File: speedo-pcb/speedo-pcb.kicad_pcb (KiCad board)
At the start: 4 copper layers, 52 x 52 mm, 60 parts, among them J1 Debug, J2 Mode, J3 Speedo, J4 Power, J5 VBAT, J6 BOOT, J7 Breakout, M1 X27_128, U1 XC6206P332MR, U3 OLED_128x32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

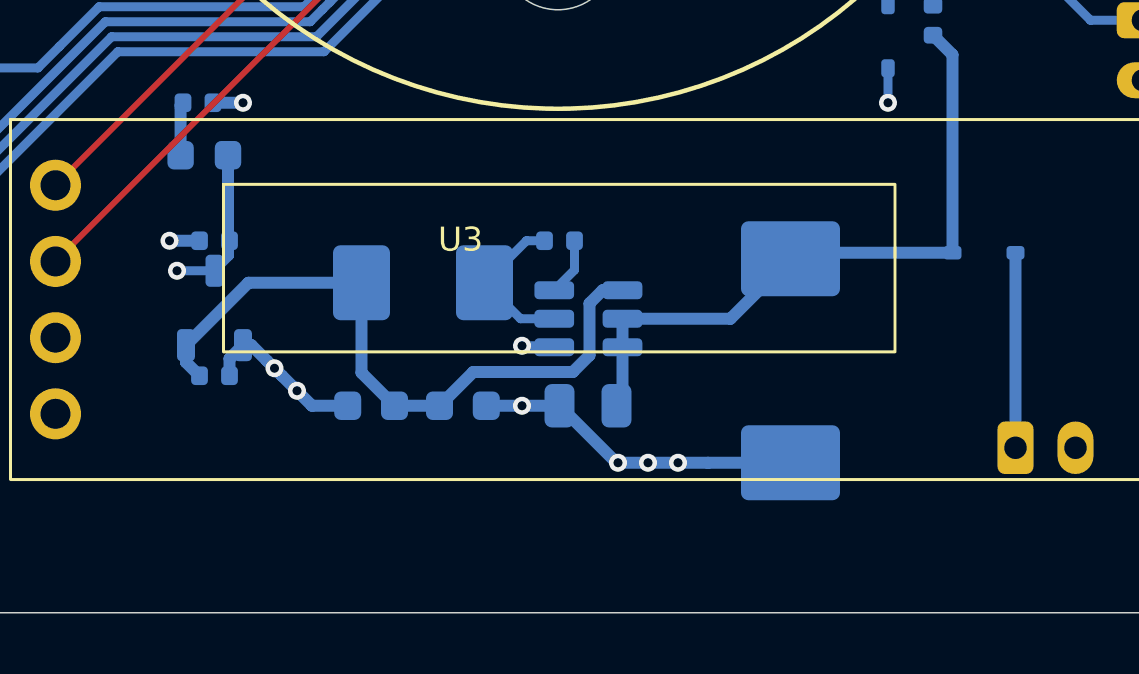
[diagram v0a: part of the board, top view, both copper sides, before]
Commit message: buck converter and tvs
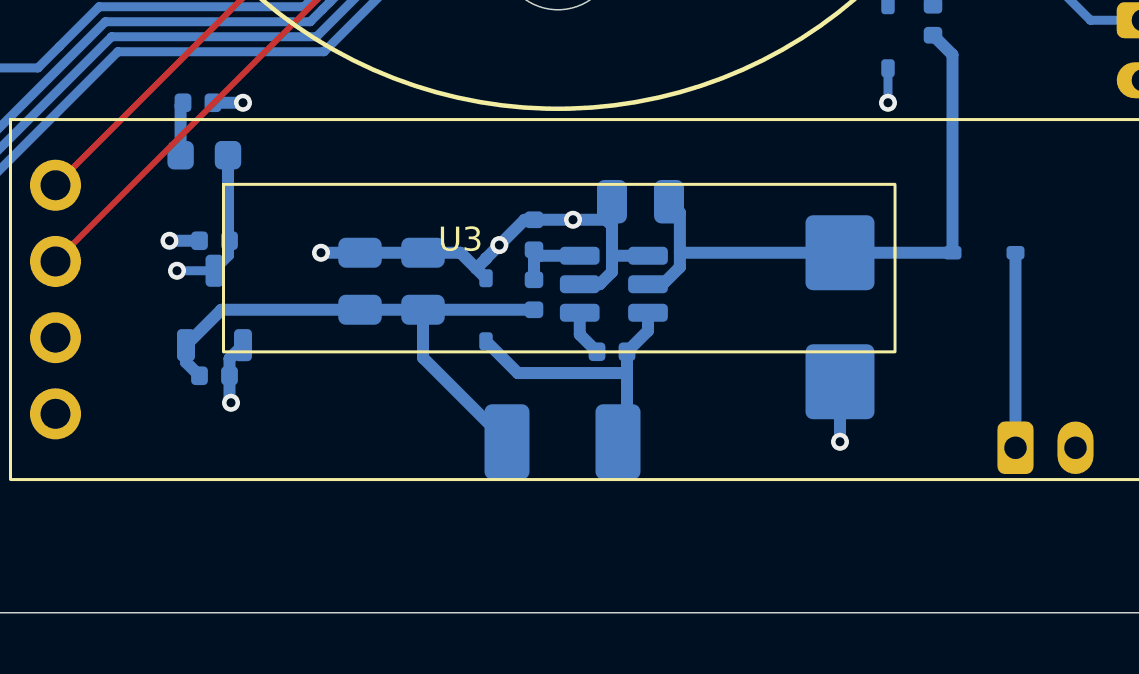
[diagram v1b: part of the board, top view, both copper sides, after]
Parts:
- removed C6: 22uF, PCM_JLCPCB:C_0603
- removed L2: 4.7uH, Inductor_SMD:L_Chilisin_BMRA00050520
- removed U5: AP63205WU, Package_TO_SOT_SMD:TSOT-23-6
- added C20: 22uF, PCM_JLCPCB:C_0805, B.Cu at (93.4, 115.0)
- added D14: P6SMB6.8CA/TR13, PCM_JLCPCB:D_SMB, B.Cu at (109.4, 116.2)
- added L1: FXL0420-100-M, Inductor_SMD:L_Sunlord_MWSA0402S, B.Cu at (100.2, 120.3)
- added R4: 10kΩ, PCM_JLCPCB:R_0402, B.Cu at (99.2, 115.4)
- added R7: 2kΩ, PCM_JLCPCB:R_0402, B.Cu at (99.2, 113.4)
- added U6: LGS5145, Package_TO_SOT_SMD:SOT-23-6, B.Cu at (101.9, 115.0)
- C5: value 22uF -> 10uF; footprint PCM_JLCPCB:C_0603 -> PCM_JLCPCB:C_0805
- D12: value SMCJ18CA -> 1N5819WS; footprint PCM_JLCPCB:D_SMC -> PCM_JLCPCB:D_SOD-323
- moved D12 10.3 mm to (97.6, 115.9)
- moved C4 7.02 mm to (102.8, 112.3)
- moved C5 4.36 mm to (95.5, 115.0), turned to 90 degrees
- moved C1 4.09 mm to (101.8, 117.3)
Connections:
- C1 pad 2: Net-(U5-BST) -> Net-(U6-SW)
- D12 pad 1: GND -> Net-(U6-SW)
- D12 pad 2: +12V -> GND
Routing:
- net Net-(U6-SW): track 0.00 -> 9.86 mm
- net Net-(U6-BST): track 5.40 -> 1.54 mm
- net +5V: track 22.7 -> 18.9 mm
- net Net-(U6-FB): track 0.00 -> 2.61 mm
- net GND: track 51.1 -> 53.6 mm, vias 24 -> 22
- net Net-(U5-BST): track 1.93 -> 0.00 mm
- net +12V: track 22.1 -> 20.2 mm

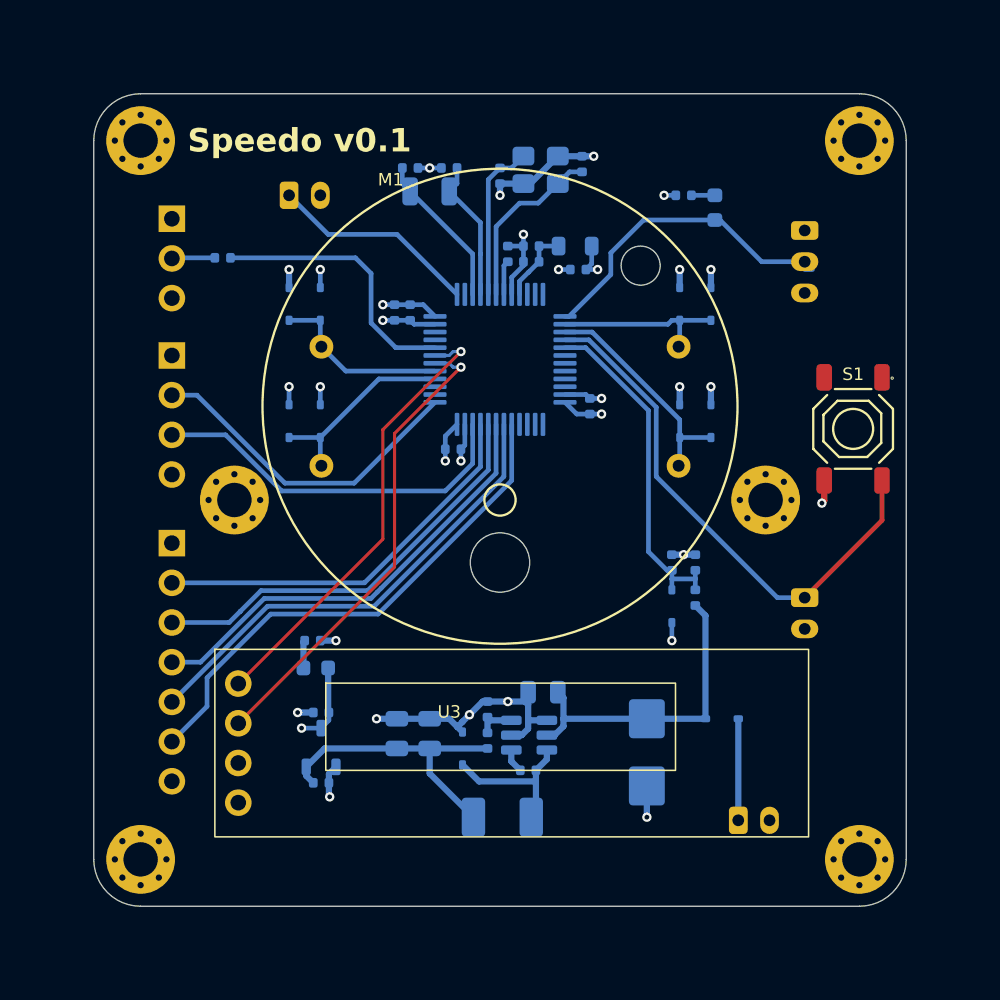
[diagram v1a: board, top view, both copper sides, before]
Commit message: buck converter fills
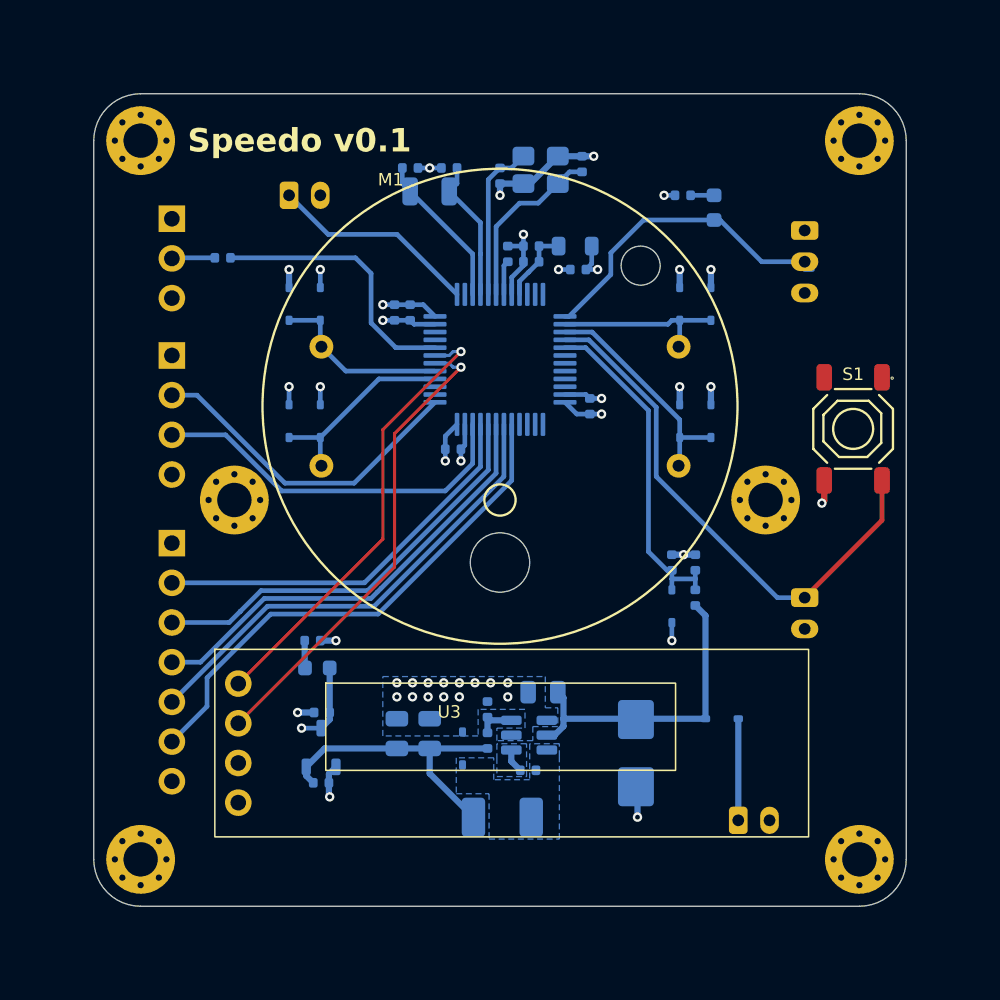
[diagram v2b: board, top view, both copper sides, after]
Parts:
- removed D10: Green, PCM_JLCPCB:D_0603
- added D15: Red, PCM_JLCPCB:D_0603, B.Cu at (113.7, 81.3)
- R1: value 33Ω -> 51Ω
- moved D14 0.70 mm to (108.7, 116.2)
- moved D11 0.10 mm to (88.3, 110.8)
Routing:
- net GND: track 53.6 -> 37.7 mm, vias 22 -> 33
- net Net-(U6-SW): track 9.86 -> 0.42 mm
- added copper zone on B.Cu, net GND
- added copper zone on B.Cu, net Net-(U6-BST)
- added copper zone on B.Cu, net Net-(U6-SW)

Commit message: fix drc issue
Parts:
- moved C17 0.20 mm to (88.6, 113.4)
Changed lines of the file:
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@@
 	(footprint "PCM_JLCPCB:C_0402"
 		(layer "B.Cu")
-		(at 88.6 113.6 180)
+		(at 88.6 113.4 180)
 		(descr "Capacitor SMD 0402 (1005 Metric), square (rectangular) end terminal, IPC_7351 nominal, (Body size source: IPC-SM-782 page 76, https://www.pcb-3d.com/wordpress/wp-content/uploads/ipc-sm-782a_amendment_1_and_2.pdf), generated with kicad-footprint-generator")
 		(tags "capacitor")
@@
 	)
 	(via
-		(at 87.05 113.6)
+		(at 87.05 113.4)
 		(size 0.6)
 		(drill 0.3)
@@
 	)
 	(segment
-		(start 88.05 113.6)
-		(end 87.05 113.6)
+		(start 88.05 113.4)
+		(end 87.05 113.4)
 		(width 0.4)
 		(layer "B.Cu")
@@
 		(priority 4)
 		(connect_pads yes
-			(clearance 0.2)
+			(clearance 0.21)
 		)
 		(min_thickness 0.25)

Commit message: change tvs
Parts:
- removed D14: P6SMB6.8CA/TR13, PCM_JLCPCB:D_SMB
- added D10: SMAJ16A, PCM_JLCPCB:D_SMA, B.Cu at (108.0, 116.0)
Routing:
- net GND: track 37.7 -> 38.2 mm

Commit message: fix buck en pin
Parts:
- moved D10 1.70 mm to (108.0, 114.3)
- moved D13 1.70 mm to (114.2, 112.3)
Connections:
- U6 pad 4: GND -> +12V
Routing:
- net GND: track 38.2 -> 35.7 mm, vias 33 -> 32
- net +12V: track 20.2 -> 18.3 mm
- net Net-(J4-Pin_1): track 6.50 -> 8.20 mm
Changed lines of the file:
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@@
 			)
 		)
-		(property "Stock" "9266857"
+		(property "Stock" "8534728"
 			(at 0 0 90)
 			(unlocked yes)
@@
 			)
 		)
-		(property "Stock" "2307117"
+		(property "Stock" "2112966"
 			(at 0 0 0)
 			(unlocked yes)
@@
 			)
 		)
-		(property "Stock" "28090188"
+		(property "Stock" "26683372"
 			(at 0 0 -90)
 			(unlocked yes)
@@
 			)
 		)
-		(property "Stock" "475295"
+		(property "Stock" "460537"
 			(at 0 0 180)
 			(unlocked yes)
@@
 			)
 		)
-		(property "Stock" "2351029"
+		(property "Stock" "2164219"
 			(at 0 0 90)
 			(unlocked yes)
@@
 			)
 		)
-		(property "Stock" "8425249"
+		(property "Stock" "7930855"
 			(at 0 0 0)
 			(unlocked yes)
@@
 			)
 		)
-		(property "Stock" "8425249"
+		(property "Stock" "7930855"
 			(at 0 0 0)
 			(unlocked yes)
@@
 			)
 		)
-		(property "Stock" "842329"
+		(property "Stock" "753654"
 			(at 0 0 180)
 			(unlocked yes)
@@
 			)
 		)
-		(property "Stock" "28090188"
+		(property "Stock" "26683372"
 			(at 0 0 180)
 			(unlocked yes)
@@
 			)
 		)
-		(property "Stock" "28090188"
+		(property "Stock" "26683372"
 			(at 0 0 -90)
 			(unlocked yes)
@@
 			)
 		)
-		(property "Stock" "6919009"
+		(property "Stock" "5699128"
 			(at 0 0 0)
 			(unlocked yes)
@@
 			)
 		)
-		(property "Stock" "1000891"
+		(property "Stock" "981408"
 			(at 0 0 0)
 			(unlocked yes)
@@
 			)
 		)
-		(property "Stock" "432692"
+		(property "Stock" "388678"
 			(at 0 0 90)
 			(unlocked yes)
@@
 			)
 		)
-		(property "Stock" "156631"
+		(property "Stock" "226209"
 			(at 0 0 90)
 			(unlocked yes)
@@
 			)
 		)
-		(property "Stock" "842329"
+		(property "Stock" "753654"
 			(at 0 0 0)
 			(unlocked yes)
@@
 	(footprint "PCM_JLCPCB:D_SOD-323"
 		(layer "B.Cu")
-		(at 114.2 114)
+		(at 114.2 112.3)
 		(descr "SOD-323")
 		(tags "SOD-323")
@@
 			)
 		)
-		(property "Stock" "671957"
+		(property "Stock" "613212"
 			(at 0 0 -90)
 			(unlocked yes)
@@
 			)
 		)
-		(property "Stock" "228988"
+		(property "Stock" "216941"
 			(at 0 0 0)
 			(unlocked yes)
@@
 			)
 		)
-		(property "Stock" "5578116"
+		(property "Stock" "5031445"
 			(at 0 0 -90)
 			(unlocked yes)
@@
 			)
 		)
-		(property "Stock" "28090188"
+		(property "Stock" "26683372"
 			(at 0 0 90)
 			(unlocked yes)
@@
 			)
 		)
-		(property "Stock" "952916"
+		(property "Stock" "882441"
 			(at 0 0 -90)
 			(unlocked yes)
@@
 			(layers "B.Cu" "B.Paste" "B.Mask")
 			(roundrect_rratio 0.25)
-			(net 7 "GND")
+			(net 15 "+12V")
 			(pinfunction "EN")
 			(pintype "input")
@@
 	(footprint "PCM_JLCPCB:D_SMA"
 		(layer "B.Cu")
-		(at 108 116 -90)
+		(at 108 114.3 -90)
 		(descr "Diode SMA (DO-214AC)")
 		(tags "Diode SMA (DO-214AC)")
@@
 			)
 		)
-		(property "Stock" "28090188"
+		(property "Stock" "26683372"
 			(at 0 0 90)
 			(unlocked yes)
@@
 			)
 		)
-		(property "Stock" "432692"
+		(property "Stock" "388678"
 			(at 0 0 -90)
 			(unlocked yes)
@@
 			)
 		)
-		(property "Stock" "313046"
+		(property "Stock" "304118"
 			(at 0 0 180)
 			(unlocked yes)
@@
 	)
 	(via
-		(at 108 120.5)
-		(size 0.6)
-		(drill 0.3)
-		(layers "F.Cu" "B.Cu")
-		(net 7)
-	)
-	(via
 		(at 100 80.5)
 		(size 0.6)
@@
 	)
 	(segment
-		(start 108 118)
-		(end 108 120.5)
-		(width 0.4)
-		(layer "B.Cu")
-		(net 7)
-	)
-	(segment
 		(start 112.5 103.5)
 		(end 111.75 103.5)
@@
 	)
 	(segment
-		(start 103.494474 115.05)
-		(end 104.0625 114.481974)
+		(start 103.7 113.4)
+		(end 103 114.1)
 		(width 0.4)
 		(layer "B.Cu")
@@
 	)
 	(segment
-		(start 113.15 114)
-		(end 113.15 107.4)
-		(width 0.4)
-		(layer "B.Cu")
-		(net 15)
-	)
-	(segment
-		(start 113.15 114)
-		(end 109.4 114)
-		(width 0.4)
-		(layer "B.Cu")
-		(net 15)
-	)
-	(segment
-		(start 104.0625 114)
-		(end 104.0625 112.6625)
+		(start 108 112.3)
+		(end 103.7 112.3)
 		(width 0.4)
 		(layer "B.Cu")
@@
 	)
 	(segment
-		(start 103 115.05)
-		(end 103.494474 115.05)
+		(start 103.7 112.3)
+		(end 103.7 113.4)
 		(width 0.4)
 		(layer "B.Cu")
@@
 	)
 	(segment
-		(start 109.4 114)
-		(end 104.0625 114)
+		(start 113.15 107.4)
+		(end 113.15 112.3)
 		(width 0.4)
 		(layer "B.Cu")
@@
 	)
 	(segment
-		(start 104.0625 112.6625)
-		(end 103.7 112.3)
+		(start 103 114.1)
+		(end 103 115.05)
 		(width 0.4)
 		(layer "B.Cu")
@@
 	)
 	(segment
-		(start 104.0625 114.481974)
-		(end 104.0625 114)
+		(start 113.15 112.3)
+		(end 108 112.3)
 		(width 0.4)
 		(layer "B.Cu")
@@
 	)
 	(segment
-		(start 115.25 120.5)
-		(end 115.25 114)
+		(start 115.25 112.3)
+		(end 115.25 120.5)
 		(width 0.4)
 		(layer "B.Cu")
@@
 			)
 		)
+	)
+	(zone
+		(net 7)
+		(net_name "GND")
+		(layer "B.Cu")
+		(hatch edge 0.5)
+		(priority 5)
+		(connect_pads
+			(clearance 0.21)
+		)
+		(min_thickness 0.25)
+		(filled_areas_thickness no)
+		(fill yes
+			(thermal_gap 0.5)
+			(thermal_bridge_width 0.5)
+		)
+		(polygon
+			(pts
+				(xy 130 70) (xy 70 70) (xy 70 130) (xy 130 130)
+			)
+		)

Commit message: pcb cleanup
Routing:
- net Net-(U6-SW): track 0.42 -> 9.97 mm
- net GND: vias 32 -> 18
- removed copper zone on B.Cu, net Net-(U6-SW)

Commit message: oled decoupling capacitor and i2c pull up resistors
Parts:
- added C6: 100nF, PCM_JLCPCB:C_0402, B.Cu at (84.8, 117.3)
- added R8: 4.7kΩ, PCM_JLCPCB:R_0402, B.Cu at (84.8, 113.8)
- added R9: 4.7kΩ, PCM_JLCPCB:R_0402, B.Cu at (84.8, 111.2)
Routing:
- net +3.3V: track 22.5 -> 25.9 mm, vias 10 -> 12
- net GND: track 35.7 -> 37.9 mm
- net SDA: track 28.9 -> 30.5 mm
- net SCK: track 30.5 -> 32.0 mm
